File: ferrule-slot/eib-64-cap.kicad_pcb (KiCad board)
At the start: 2 copper layers, 140.4 x 111.2 mm, 48 parts, among them J1 DF40C-70DP-0.4V(51), J10 DF40C-70DP-0.4V(51), J11 DF40C-70DP-0.4V(51), J12 DF40C-70DP-0.4V(51), J2 DF40C-70DP-0.4V(51), J3 DF40C-70DP-0.4V(51), J4 DF40C-70DP-0.4V(51), J5 DF40C-70DP-0.4V(51), J6 DF40C-70DP-0.4V(51), J7 DF40C-70DP-0.4V(51)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

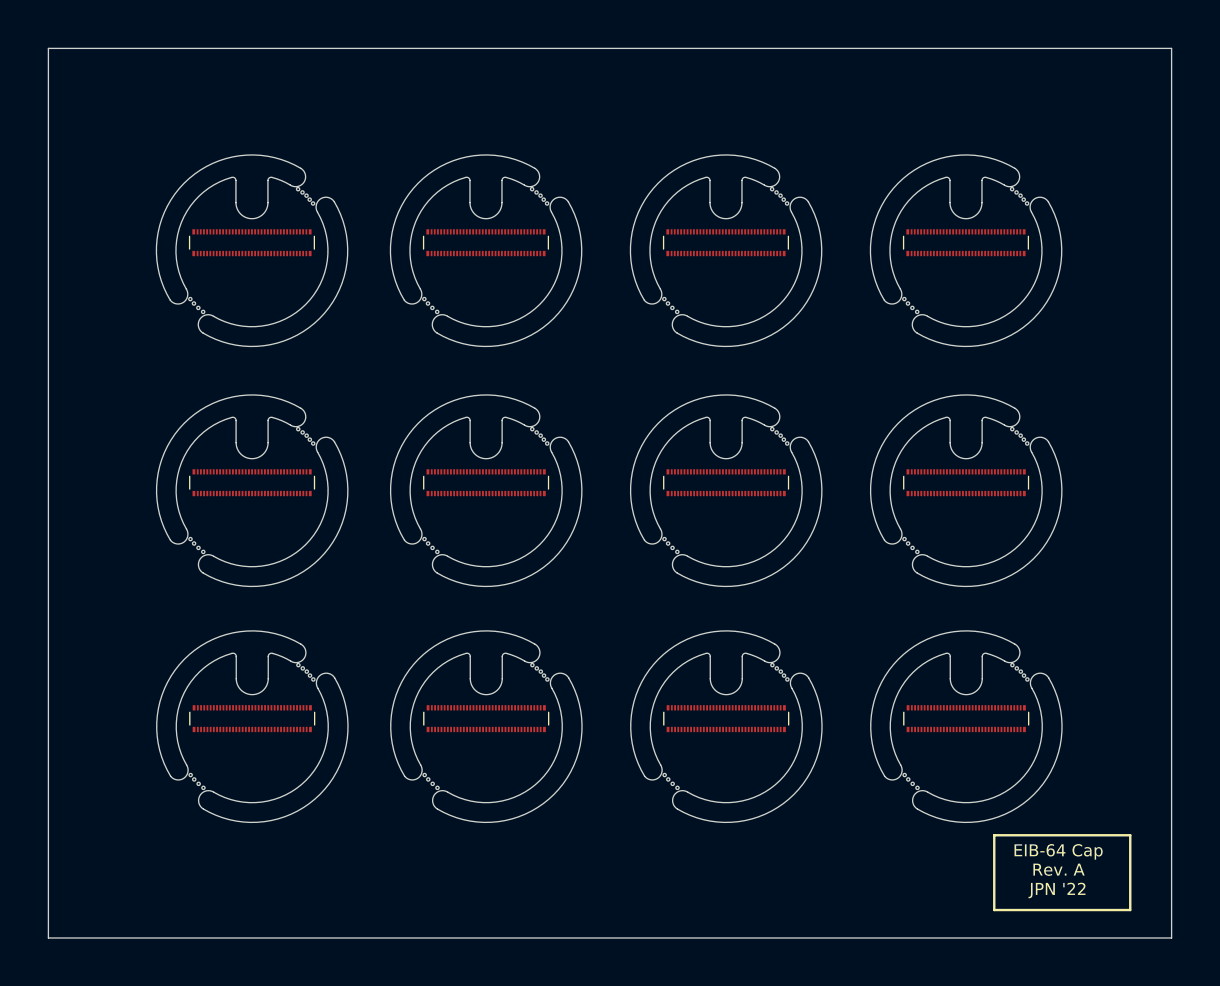
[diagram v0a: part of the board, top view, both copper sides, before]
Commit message: Add hats to EIB cap with ferrule
- Remove copper from mouse bites to prevent burs
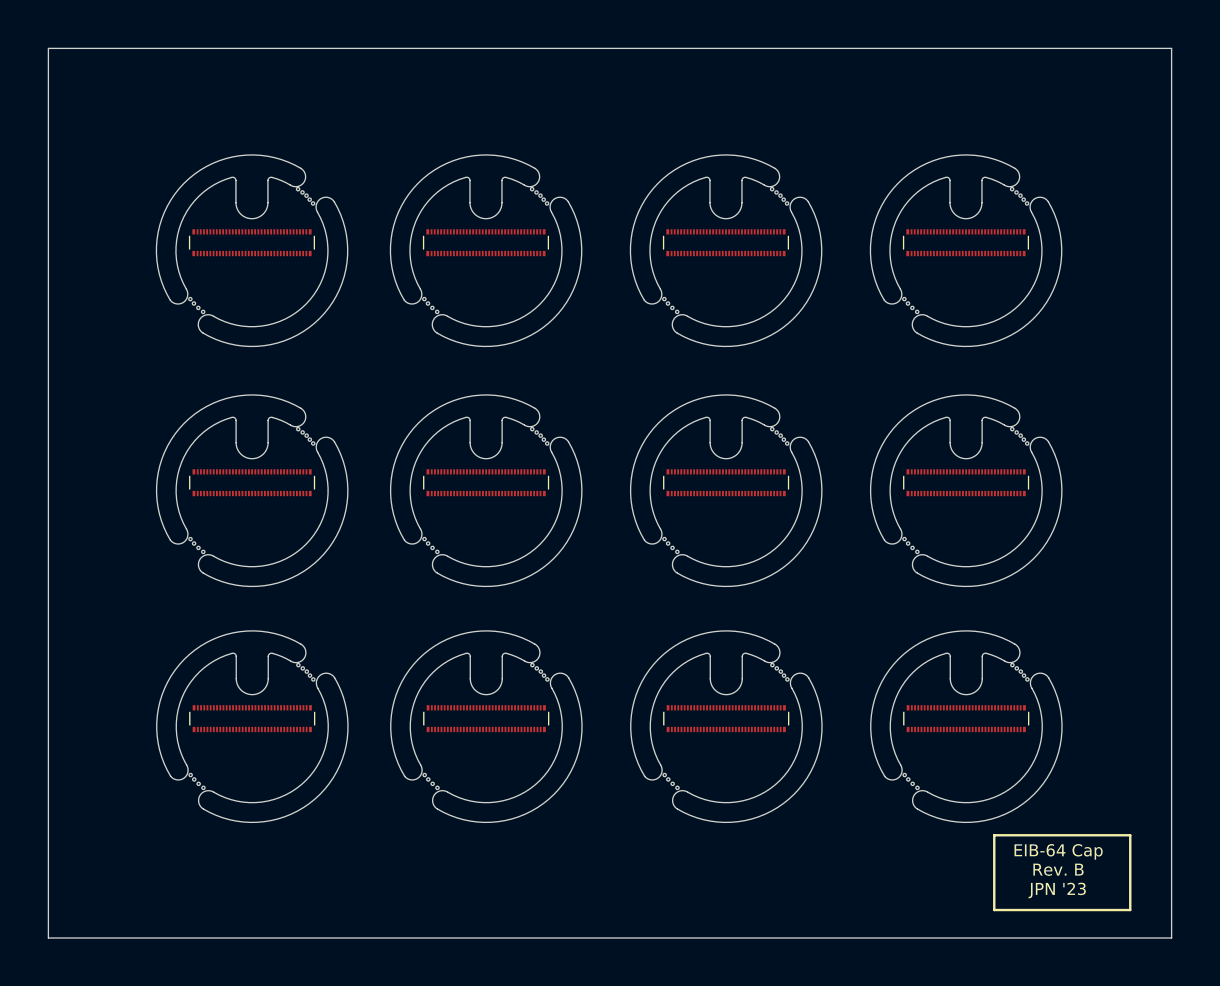
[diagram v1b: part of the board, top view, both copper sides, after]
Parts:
- removed the G*** at (81.3, 73.6)
- removed the G*** at (171.3, 133.2)
- removed the G*** at (171.3, 73.6)
- removed the G*** at (141.3, 103.4)
- removed the G*** at (172.3, 133.1)
- removed the G*** at (82.2, 68.0)
- removed the G*** at (82.3, 97.7)
- removed the G*** at (111.8, 127.3)
- removed the G*** at (142.3, 68.0)
- removed the G*** at (82.3, 73.5)
- removed the G*** at (112.3, 97.7)
- removed the G*** at (171.3, 103.4)
- removed the G*** at (82.3, 103.3)
- removed the G*** at (112.3, 103.3)
- removed the G*** at (142.3, 97.7)
- removed the G*** at (171.5, 97.7)
- removed the G*** at (142.3, 73.5)
- removed the G*** at (82.3, 133.1)
- removed the G*** at (112.3, 133.1)
- removed the G*** at (142.3, 103.3)
- removed the G*** at (172.3, 103.3)
- removed the G*** at (172.3, 73.5)
- removed the G*** at (141.3, 73.6)
- removed the G*** at (171.5, 127.3)
- removed the G*** at (171.6, 68.0)
- removed the G*** at (142.3, 133.1)
- removed the G*** at (112.3, 67.8)
- removed the G*** at (142.3, 127.3)
- removed the G*** at (112.3, 73.5)
- removed the G*** at (82.3, 127.3)
- removed the G*** at (111.3, 103.4)
- removed the G*** at (81.3, 103.4)
- removed the G*** at (81.3, 133.2)
- removed the G*** at (111.3, 73.6)
- removed the G*** at (111.3, 133.2)
- removed the G*** at (141.3, 133.2)
- added G***: LOGO, LOGO, F.Cu at (106.9, 93.4)
- added G***: LOGO, LOGO, F.Cu at (137.0, 93.5)
- added G***: LOGO, LOGO, F.Cu at (77.7, 93.3)
- added G***: LOGO, LOGO, F.Cu at (141.7, 102.7)
- added G***: LOGO, LOGO, F.Cu at (107.0, 122.9)
- added G***: LOGO, LOGO, F.Cu at (82.1, 72.8)
- added G***: LOGO, LOGO, F.Cu at (77.7, 63.3)
- added G***: LOGO, LOGO, F.Cu at (111.9, 102.7)
- added G***: LOGO, LOGO, F.Cu at (167.0, 63.4)
- added G***: LOGO, LOGO, F.Cu at (171.5, 132.3)
- added G***: LOGO, LOGO, F.Cu at (137.0, 63.4)
- added G***: LOGO, LOGO, F.Cu at (171.5, 102.7)
- added G***: LOGO, LOGO, F.Cu at (111.9, 132.3)
- added G***: LOGO, LOGO, F.Cu at (111.9, 72.8)
- added G***: LOGO, LOGO, F.Cu at (171.5, 72.8)
- added G***: LOGO, LOGO, F.Cu at (166.9, 122.9)
- added G***: LOGO, LOGO, F.Cu at (82.1, 132.3)
- added G***: LOGO, LOGO, B.Cu at (82.2, 71.2)
- added G***: LOGO, LOGO, B.Cu at (111.6, 71.0)
- added G***: LOGO, LOGO, B.Cu at (141.6, 100.8)
- added G***: LOGO, LOGO, B.Cu at (142.4, 129.9)
- added G***: LOGO, LOGO, B.Cu at (82.6, 129.8)
- added G***: LOGO, LOGO, F.Cu at (167.0, 93.4)
- added G***: LOGO, LOGO, B.Cu at (172.3, 130.5)
- added G***: LOGO, LOGO, B.Cu at (111.5, 130.6)
- added G***: LOGO, LOGO, B.Cu at (171.9, 100.7)
- added G***: LOGO, LOGO, B.Cu at (171.5, 70.6)
- added G***: LOGO, LOGO, B.Cu at (141.8, 70.3)
- added G***: LOGO, LOGO, B.Cu at (82.1, 100.8)
- added G***: LOGO, LOGO, B.Cu at (111.2, 100.2)
- added G***: LOGO, LOGO, F.Cu at (137.1, 123.1)
- added G***: LOGO, LOGO, F.Cu at (141.7, 132.3)
- added G***: LOGO, LOGO, F.Cu at (82.1, 102.7)
- added G***: LOGO, LOGO, F.Cu at (107.0, 63.3)
- added G***: LOGO, LOGO, F.Cu at (77.7, 122.9)
- added G***: LOGO, LOGO, F.Cu at (141.7, 72.8)
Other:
- board text added: "EIB-64 Cap Rev. B JPN '23"
- board text removed: "EIB-64 Cap Rev. A JPN '22"

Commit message: Updated caps.
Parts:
- removed the G*** at (141.7, 102.7)
- removed the G*** at (82.1, 72.8)
- removed the G*** at (111.9, 102.7)
- removed the G*** at (171.5, 132.3)
- removed the G*** at (171.5, 102.7)
- removed the G*** at (111.9, 132.3)
- removed the G*** at (111.9, 72.8)
- removed the G*** at (171.5, 72.8)
- removed the G*** at (82.1, 132.3)
- removed the G*** at (141.7, 132.3)
- removed the G*** at (82.1, 102.7)
- removed the G*** at (141.7, 72.8)
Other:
- board text added: "EIB-64 Cap Rev. C JPN '25"
- board text added: "open-ephys.org"
- board text removed: "EIB-64 Cap Rev. B JPN '23"
